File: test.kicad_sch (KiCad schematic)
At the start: 2 parts, among them J1 Conn_01x44_Socket, J2 Conn_01x44_Socket

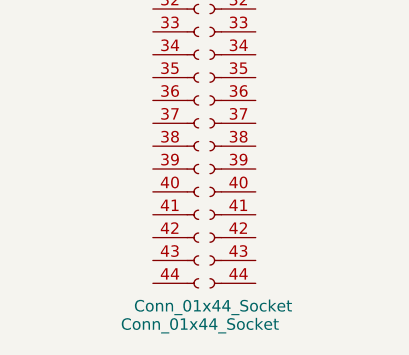
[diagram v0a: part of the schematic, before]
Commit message: 添加两个地并连线
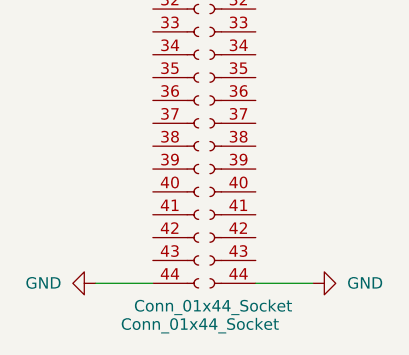
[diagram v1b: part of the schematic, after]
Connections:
- net GND: now reaches J1.44 (Pin_44)
- net GND: now also J2.44 (Pin_44)
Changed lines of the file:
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@@
 	(generator_version "8.0")
 	(paper "A4")
+	(wire
+		(pts
+			(xy 29.21 139.7) (xy 35.56 139.7)
+		)
+		(stroke
+			(width 0)
+			(type default)
+		)
+	)
+	(wire
+		(pts
+			(xy 46.99 139.7) (xy 53.34 139.7)
+		)
+		(stroke
+			(width 0)
+			(type default)
+		)
+	)
+	(symbol
+		(lib_id "power:GND")
+		(at 29.21 139.7 270)
+		(unit 1)
+		(exclude_from_sim no)
+		(in_bom yes)
+		(on_board yes)
+		(dnp no)
+		(fields_autoplaced yes)
+		(property "Reference" "#PWR02"
+			(at 22.86 139.7 0)
+			(effects
+				(font
+					(size 1.27 1.27)
+				)
+				(hide yes)
+			)
+		)
+		(property "Value" "GND"
+			(at 25.4 139.6999 90)
+			(effects
+				(font
+					(size 1.27 1.27)
+				)
+				(justify right)
+			)
+		)
+		(property "Footprint" ""
+			(at 29.21 139.7 0)
+			(effects
+				(font
+					(size 1.27 1.27)
+				)
+				(hide yes)
+			)
+		)
+		(property "Datasheet" ""
+			(at 29.21 139.7 0)
+			(effects
+				(font
+					(size 1.27 1.27)
+				)
+				(hide yes)
+			)
+		)
+		(property "Description" "Power symbol creates a global label with name \"GND\" , ground"
+			(at 29.21 139.7 0)
+			(effects
+				(font
+					(size 1.27 1.27)
+				)
+				(hide yes)
+			)
+		)
+		(pin "1"
+		)
+		(instances
+			(project ""
+				(path "/208ebb94-da73-40e8-b1b0-b08490f18890"
+					(reference "#PWR02")
+					(unit 1)
+				)
+			)
+		)
+	)
 	(symbol
 		(lib_id "Connector:Conn_01x44_Socket")
@@
 					(unit 1)
 				)
+			)
+		)
+	)
+	(symbol
+		(lib_id "power:GND")
+		(at 53.34 139.7 90)
+		(unit 1)
+		(exclude_from_sim no)
+		(in_bom yes)
+		(on_board yes)
+		(dnp no)
+		(fields_autoplaced yes)
+		(property "Reference" "#PWR01"
+			(at 59.69 139.7 0)
+			(effects
+				(font
+					(size 1.27 1.27)
+				)
+				(hide yes)
+			)
+		)
+		(property "Value" "GND"
+			(at 57.15 139.6999 90)
+			(effects
+				(font
+					(size 1.27 1.27)
+				)
+				(justify right)
+			)
+		)
+		(property "Footprint" ""
+			(at 53.34 139.7 0)
+			(effects
+				(font
+					(size 1.27 1.27)
+				)
+				(hide yes)
+			)
+		)
+		(property "Datasheet" ""
+			(at 53.34 139.7 0)
+			(effects
+				(font
+					(size 1.27 1.27)
+				)
+				(hide yes)
+			)
+		)
+		(property "Description" "Power symbol creates a global label with name \"GND\" , ground"
+			(at 53.34 139.7 0)
+			(effects
+				(font
+					(size 1.27 1.27)
+				)
+				(hide yes)
+			)
+		)
+		(pin "1"
+		)
+		(instances
+			(project ""
+				(path "/208ebb94-da73-40e8-b1b0-b08490f18890"
+					(reference "#PWR01")
+					(unit 1)
+				)
